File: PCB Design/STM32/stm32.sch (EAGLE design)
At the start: 68 parts, among them IC1 NCP1117ST50T3G, Q1 8MHz, T1 SFH303, T2 SFH303, T3 SFH303, T4 SFH303, U1 STM32F103RET6, U2 MCP1700T-3302E/TT, U3 MCP1700T-3302E/TT, U4 MPU-6050, U5 TB6612FNG, X1 22-23-2031

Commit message: first darft
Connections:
- net IR_OUT1: now also U1.PC9; no longer U1.PC6
- net IR_OUT2: now also U1.PC8; no longer U1.PC7
- net IR_OUT3: now also U1.PC7; no longer U1.PC8
- net IR_OUT4: now also U1.PC6; no longer U1.PC9
- net M1CA: now also JP4.6; no longer JP3.6
- net M1CB: now also JP4.5; no longer JP3.5
- net M2CA: now also JP3.6, U1.PB15; no longer JP4.6, U1.PB14
- net M2CB: now also JP3.5, U1.PB14; no longer JP4.5, U1.PB15
- net USART1_RX: now also U$1.6; no longer U$1.4
- net USART1_TX: now also U$1.4; no longer U$1.6
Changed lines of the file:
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@@
+</segment>
+<segment>
+<wire x1="99.06" y1="172.72" x2="109.22" y2="172.72" width="0.1524" layer="91"/>
+<label x="99.06" y="172.72" size="1.778" layer="95"/>
+<pinref part="U$1" gate="G$1" pin="6"/>
+</segment>
+</net>
+<net name="USART1_TX" class="0">
+<segment>
+<wire x1="162.56" y1="215.9" x2="147.32" y2="215.9" width="0.1524" layer="91"/>
+<label x="142.24" y="215.9" size="1.778" layer="95"/>
+<pinref part="U1" gate="A" pin="PA9"/>
 </segment>
 <segment>
@@
 <label x="99.06" y="175.26" size="1.778" layer="95"/>
 <pinref part="U$1" gate="G$1" pin="4"/>
-</segment>
-</net>
-<net name="USART1_TX" class="0">
-<segment>
-<wire x1="162.56" y1="215.9" x2="147.32" y2="215.9" width="0.1524" layer="91"/>
-<label x="142.24" y="215.9" size="1.778" layer="95"/>
-<pinref part="U1" gate="A" pin="PA9"/>
-</segment>
-<segment>
-<wire x1="99.06" y1="172.72" x2="109.22" y2="172.72" width="0.1524" layer="91"/>
-<label x="99.06" y="172.72" size="1.778" layer="95"/>
-<pinref part="U$1" gate="G$1" pin="6"/>
 </segment>
 </net>
@@
 </segment>
 <segment>
+<pinref part="U1" gate="A" pin="PC8"/>
+<wire x1="223.52" y1="226.06" x2="238.76" y2="226.06" width="0.1524" layer="91"/>
+<label x="228.6" y="226.06" size="1.778" layer="95"/>
+</segment>
+</net>
+<net name="IR_OUT1" class="0">
+<segment>
+<pinref part="R11" gate="G$1" pin="2"/>
+<wire x1="259.08" y1="236.22" x2="259.08" y2="226.06" width="0.1524" layer="91"/>
+<label x="259.08" y="228.6" size="1.778" layer="95"/>
+</segment>
+<segment>
+<pinref part="U1" gate="A" pin="PC9"/>
+<wire x1="223.52" y1="223.52" x2="238.76" y2="223.52" width="0.1524" layer="91"/>
+<label x="228.6" y="223.52" size="1.778" layer="95"/>
+</segment>
+</net>
+<net name="IR_OUT3" class="0">
+<segment>
+<pinref part="R13" gate="G$1" pin="2"/>
+<wire x1="304.8" y1="236.22" x2="304.8" y2="226.06" width="0.1524" layer="91"/>
+<label x="304.8" y="228.6" size="1.778" layer="95"/>
+</segment>
+<segment>
 <pinref part="U1" gate="A" pin="PC7"/>
 <wire x1="223.52" y1="228.6" x2="238.76" y2="228.6" width="0.1524" layer="91"/>
 <label x="228.6" y="228.6" size="1.778" layer="95"/>
-</segment>
-</net>
-<net name="IR_OUT1" class="0">
-<segment>
-<pinref part="R11" gate="G$1" pin="2"/>
-<wire x1="259.08" y1="236.22" x2="259.08" y2="226.06" width="0.1524" layer="91"/>
-<label x="259.08" y="228.6" size="1.778" layer="95"/>
-</segment>
-<segment>
-<pinref part="U1" gate="A" pin="PC6"/>
-<wire x1="223.52" y1="231.14" x2="238.76" y2="231.14" width="0.1524" layer="91"/>
-<label x="228.6" y="231.14" size="1.778" layer="95"/>
-</segment>
-</net>
-<net name="IR_OUT3" class="0">
-<segment>
-<pinref part="R13" gate="G$1" pin="2"/>
-<wire x1="304.8" y1="236.22" x2="304.8" y2="226.06" width="0.1524" layer="91"/>
-<label x="304.8" y="228.6" size="1.778" layer="95"/>
-</segment>
-<segment>
-<pinref part="U1" gate="A" pin="PC8"/>
-<wire x1="223.52" y1="226.06" x2="238.76" y2="226.06" width="0.1524" layer="91"/>
-<label x="228.6" y="226.06" size="1.778" layer="95"/>
 </segment>
 </net>
@@
 </segment>
 <segment>
-<pinref part="U1" gate="A" pin="PC9"/>
-<wire x1="223.52" y1="223.52" x2="238.76" y2="223.52" width="0.1524" layer="91"/>
-<label x="228.6" y="223.52" size="1.778" layer="95"/>
+<pinref part="U1" gate="A" pin="PC6"/>
+<wire x1="223.52" y1="231.14" x2="238.76" y2="231.14" width="0.1524" layer="91"/>
+<label x="228.6" y="231.14" size="1.778" layer="95"/>
 </segment>
 </net>
@@
 <net name="M1CB" class="0">
 <segment>
+<wire x1="162.56" y1="162.56" x2="147.32" y2="162.56" width="0.1524" layer="91"/>
+<label x="154.94" y="162.56" size="1.778" layer="95" rot="MR0"/>
+<pinref part="U1" gate="A" pin="PB13"/>
+</segment>
+<segment>
+<pinref part="JP4" gate="G$1" pin="5"/>
+<wire x1="401.32" y1="109.22" x2="393.7" y2="109.22" width="0.1524" layer="91"/>
+<label x="393.7" y="106.68" size="1.778" layer="95"/>
+</segment>
+</net>
+<net name="M1CA" class="0">
+<segment>
+<wire x1="162.56" y1="165.1" x2="147.32" y2="165.1" width="0.1524" layer="91"/>
+<label x="154.94" y="165.1" size="1.778" layer="95" rot="MR0"/>
+<pinref part="U1" gate="A" pin="PB12"/>
+</segment>
+<segment>
+<pinref part="JP4" gate="G$1" pin="6"/>
+<wire x1="416.56" y1="109.22" x2="424.18" y2="109.22" width="0.1524" layer="91"/>
+<label x="419.1" y="106.68" size="1.778" layer="95"/>
+</segment>
+</net>
+<net name="M2CA" class="0">
+<segment>
+<pinref part="JP3" gate="G$1" pin="6"/>
+<wire x1="416.56" y1="129.54" x2="424.18" y2="129.54" width="0.1524" layer="91"/>
+<label x="419.1" y="127" size="1.778" layer="95"/>
+</segment>
+<segment>
+<wire x1="162.56" y1="157.48" x2="147.32" y2="157.48" width="0.1524" layer="91"/>
+<label x="154.94" y="157.48" size="1.778" layer="95" rot="MR0"/>
+<pinref part="U1" gate="A" pin="PB15"/>
+</segment>
+</net>
+<net name="M2CB" class="0">
+<segment>
 <pinref part="JP3" gate="G$1" pin="5"/>
 <wire x1="401.32" y1="129.54" x2="393.7" y2="129.54" width="0.1524" layer="91"/>
@@
 </segment>
 <segment>
-<wire x1="162.56" y1="162.56" x2="147.32" y2="162.56" width="0.1524" layer="91"/>
-<label x="154.94" y="162.56" size="1.778" layer="95" rot="MR0"/>
-<pinref part="U1" gate="A" pin="PB13"/>
-</segment>
-</net>
-<net name="M1CA" class="0">
-<segment>
-<pinref part="JP3" gate="G$1" pin="6"/>
-<wire x1="416.56" y1="129.54" x2="424.18" y2="129.54" width="0.1524" layer="91"/>
-<label x="419.1" y="127" size="1.778" layer="95"/>
-</segment>
-<segment>
-<wire x1="162.56" y1="165.1" x2="147.32" y2="165.1" width="0.1524" layer="91"/>
-<label x="154.94" y="165.1" size="1.778" layer="95" rot="MR0"/>
-<pinref part="U1" gate="A" pin="PB12"/>
-</segment>
-</net>
-<net name="M2CA" class="0">
-<segment>
-<pinref part="JP4" gate="G$1" pin="6"/>
-<wire x1="416.56" y1="109.22" x2="424.18" y2="109.22" width="0.1524" layer="91"/>
-<label x="419.1" y="106.68" size="1.778" layer="95"/>
-</segment>
-<segment>
 <wire x1="162.56" y1="160.02" x2="147.32" y2="160.02" width="0.1524" layer="91"/>
 <label x="154.94" y="160.02" size="1.778" layer="95" rot="MR0"/>
@@
 </segment>
 </net>
-<net name="M2CB" class="0">
-<segment>
-<pinref part="JP4" gate="G$1" pin="5"/>
-<wire x1="401.32" y1="109.22" x2="393.7" y2="109.22" width="0.1524" layer="91"/>
-<label x="393.7" y="106.68" size="1.778" layer="95"/>
-</segment>
-<segment>
-<wire x1="162.56" y1="157.48" x2="147.32" y2="157.48" width="0.1524" layer="91"/>
-<label x="154.94" y="157.48" size="1.778" layer="95" rot="MR0"/>
-<pinref part="U1" gate="A" pin="PB15"/>
-</segment>
-</net>

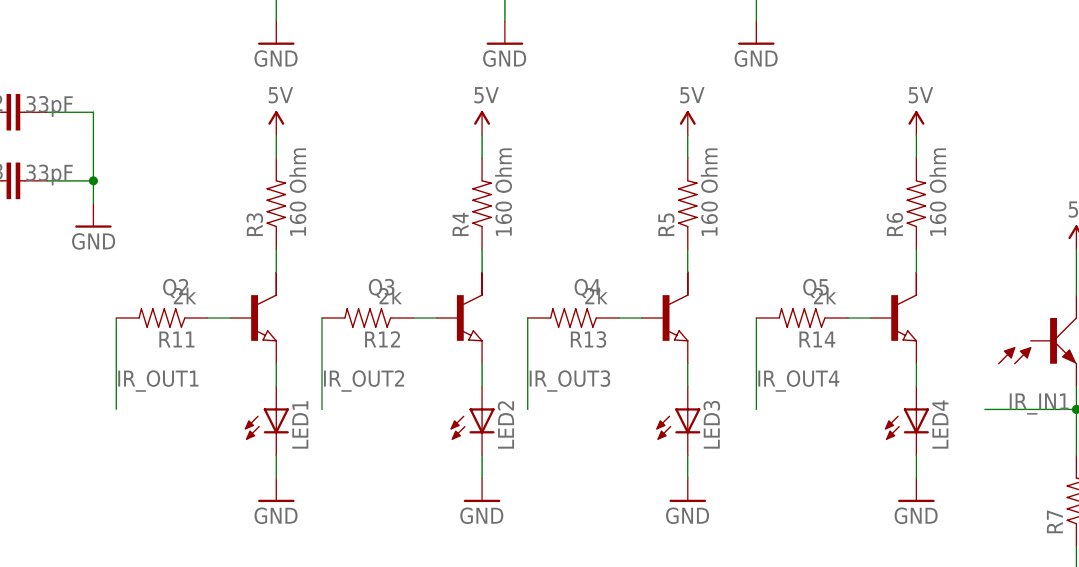
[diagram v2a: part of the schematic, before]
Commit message: changed the transistor to BC847 with package SOT23
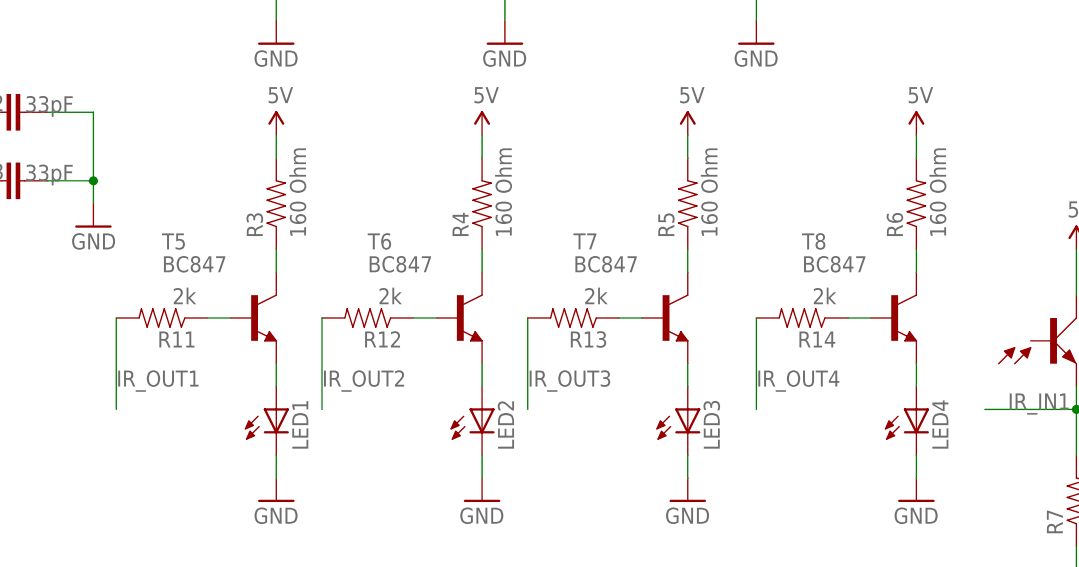
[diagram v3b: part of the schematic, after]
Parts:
- removed Q2, Q3, Q4, Q5: (no value), semicon-smd-ipc:NPN-TRANSISTIOR-2COLSOT89
- added T5, T6, T7, T8: BC847, transistor:BC847
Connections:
- net N$14: now also T8.E; no longer Q5.E
- net N$15: now also T5.C; no longer Q2.C
- net N$16: now also T7.C; no longer Q4.C
- net N$17: now also T8.C; no longer Q5.C
- net N$22: now also T8.B; no longer Q5.B
- net N$23: now also T7.B; no longer Q4.B
- net N$24: now also T6.B; no longer Q3.B
- net N$25: now also T5.B; no longer Q2.B
- net N$3: now also T6.C; no longer Q3.C
- net N$4: now also T5.E; no longer Q2.E
- net N$5: now also T6.E; no longer Q3.E
- net N$7: now also T7.E; no longer Q4.E
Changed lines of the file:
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@@
 <part name="R6" library="SparkFun-Resistors" deviceset="RESISTOR" device="0805-RES" value="160 Ohm"/>
 <part name="R10" library="SparkFun-Resistors" deviceset="RESISTOR" device="0805-RES" value="42 Ohm"/>
-<part name="Q2" library="semicon-smd-ipc" deviceset="NPN-TRANSISTIOR-2COL" device="SOT89"/>
-<part name="Q3" library="semicon-smd-ipc" deviceset="NPN-TRANSISTIOR-2COL" device="SOT89"/>
-<part name="Q4" library="semicon-smd-ipc" deviceset="NPN-TRANSISTIOR-2COL" device="SOT89"/>
-<part name="Q5" library="semicon-smd-ipc" deviceset="NPN-TRANSISTIOR-2COL" device="SOT89"/>
 <part name="GND11" library="SparkFun-Aesthetics" deviceset="GND" device=""/>
 <part name="GND14" library="SparkFun-Aesthetics" deviceset="GND" device=""/>
@@
 <part name="GND39" library="SparkFun-Aesthetics" deviceset="GND" device=""/>
 <part name="U$1" library="SparkFun-Connectors" deviceset="M04X2" device=""/>
+<part name="T5" library="transistor" deviceset="BC847" device=""/>
+<part name="T6" library="transistor" deviceset="BC847" device=""/>
+<part name="T7" library="transistor" deviceset="BC847" device=""/>
+<part name="T8" library="transistor" deviceset="BC847" device=""/>
 </parts>
 <sheets>
@@
 <instance part="R6" gate="G$1" x="347.98" y="248.92" rot="R90"/>
 <instance part="R10" gate="G$1" x="429.26" y="215.9" rot="R90"/>
-<instance part="Q2" gate="G$1" x="274.32" y="236.22"/>
-<instance part="Q3" gate="G$1" x="297.18" y="236.22"/>
-<instance part="Q4" gate="G$1" x="320.04" y="236.22"/>
-<instance part="Q5" gate="G$1" x="345.44" y="236.22"/>
 <instance part="GND11" gate="1" x="276.86" y="215.9"/>
 <instance part="GND14" gate="1" x="299.72" y="215.9"/>
@@
 <instance part="GND39" gate="1" x="101.6" y="119.38"/>
 <instance part="U$1" gate="G$1" x="91.44" y="172.72"/>
+<instance part="T5" gate="G$1" x="274.32" y="236.22"/>
+<instance part="T6" gate="G$1" x="297.18" y="236.22"/>
+<instance part="T7" gate="G$1" x="320.04" y="236.22"/>
+<instance part="T8" gate="G$1" x="345.44" y="236.22"/>
 </instances>
 <busses>
@@
 <net name="N$22" class="0">
 <segment>
-<pinref part="Q5" gate="G$1" pin="B"/>
 <pinref part="R14" gate="G$1" pin="1"/>
 <wire x1="342.9" y1="236.22" x2="340.36" y2="236.22" width="0.1524" layer="91"/>
+<pinref part="T8" gate="G$1" pin="B"/>
 </segment>
 </net>
 <net name="N$23" class="0">
 <segment>
-<pinref part="Q4" gate="G$1" pin="B"/>
 <pinref part="R13" gate="G$1" pin="1"/>
 <wire x1="317.5" y1="236.22" x2="314.96" y2="236.22" width="0.1524" layer="91"/>
+<pinref part="T7" gate="G$1" pin="B"/>
 </segment>
 </net>
 <net name="N$24" class="0">
 <segment>
-<pinref part="Q3" gate="G$1" pin="B"/>
 <pinref part="R12" gate="G$1" pin="1"/>
 <wire x1="294.64" y1="236.22" x2="292.1" y2="236.22" width="0.1524" layer="91"/>
+<pinref part="T6" gate="G$1" pin="B"/>
 </segment>
 </net>
 <net name="N$25" class="0">
 <segment>
-<pinref part="Q2" gate="G$1" pin="B"/>
 <pinref part="R11" gate="G$1" pin="1"/>
 <wire x1="271.78" y1="236.22" x2="269.24" y2="236.22" width="0.1524" layer="91"/>
+<pinref part="T5" gate="G$1" pin="B"/>
 </segment>
 </net>
@@
 <net name="N$3" class="0">
 <segment>
-<pinref part="Q3" gate="G$1" pin="C"/>
 <pinref part="R4" gate="G$1" pin="1"/>
 <wire x1="299.72" y1="243.84" x2="299.72" y2="241.3" width="0.1524" layer="91"/>
+<pinref part="T6" gate="G$1" pin="C"/>
 </segment>
 </net>
 <net name="N$4" class="0">
 <segment>
-<pinref part="Q2" gate="G$1" pin="E"/>
 <pinref part="LED1" gate="G$1" pin="A"/>
 <wire x1="276.86" y1="231.14" x2="276.86" y2="228.6" width="0.1524" layer="91"/>
+<pinref part="T5" gate="G$1" pin="E"/>
 </segment>
 </net>
 <net name="N$5" class="0">
 <segment>
-<pinref part="Q3" gate="G$1" pin="E"/>
 <pinref part="LED2" gate="G$1" pin="A"/>
 <wire x1="299.72" y1="231.14" x2="299.72" y2="228.6" width="0.1524" layer="91"/>
+<pinref part="T6" gate="G$1" pin="E"/>
 </segment>
 </net>
 <net name="N$7" class="0">
 <segment>
-<pinref part="Q4" gate="G$1" pin="E"/>
 <pinref part="LED3" gate="G$1" pin="A"/>
 <wire x1="322.58" y1="231.14" x2="322.58" y2="228.6" width="0.1524" layer="91"/>
+<pinref part="T7" gate="G$1" pin="E"/>
 </segment>
 </net>
 <net name="N$14" class="0">
 <segment>
-<pinref part="Q5" gate="G$1" pin="E"/>
 <pinref part="LED4" gate="G$1" pin="A"/>
 <wire x1="347.98" y1="231.14" x2="347.98" y2="228.6" width="0.1524" layer="91"/>
+<pinref part="T8" gate="G$1" pin="E"/>
 </segment>
 </net>
@@
 <segment>
 <pinref part="R3" gate="G$1" pin="1"/>
-<pinref part="Q2" gate="G$1" pin="C"/>
 <wire x1="276.86" y1="243.84" x2="276.86" y2="241.3" width="0.1524" layer="91"/>
+<pinref part="T5" gate="G$1" pin="C"/>
 </segment>
 </net>
@@
 <segment>
 <pinref part="R5" gate="G$1" pin="1"/>
-<pinref part="Q4" gate="G$1" pin="C"/>
 <wire x1="322.58" y1="243.84" x2="322.58" y2="241.3" width="0.1524" layer="91"/>
+<pinref part="T7" gate="G$1" pin="C"/>
 </segment>
 </net>
@@
 <segment>
 <pinref part="R6" gate="G$1" pin="1"/>
-<pinref part="Q5" gate="G$1" pin="C"/>
 <wire x1="347.98" y1="243.84" x2="347.98" y2="241.3" width="0.1524" layer="91"/>
-</segment>
-</net>
+<pinref part="T8" gate="G$1" pin="C"/>
+</segment>
+</net>

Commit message: third draft
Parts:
- C12, C13: value 33pF -> 10pF
- Q1: value 8MHz -> ABM3B-8.000MHZ-10-1UT; device SparkFun2:CRYSTAL5X3 -> SparkFun-FreqCtrl:CRYSTAL5X3
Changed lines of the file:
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@@
 </classes>
 <parts>
-<part name="Q1" library="SparkFun2" deviceset="CRYSTAL" device="5X3" value="8MHz"/>
+<part name="Q1" library="SparkFun-FreqCtrl" deviceset="CRYSTAL" device="5X3" value="ABM3B-8.000MHZ-10-1UT"/>
 <part name="GND10" library="SparkFun" deviceset="GND" device=""/>
-<part name="C12" library="SparkFun-Capacitors" deviceset="CAP" device="0805" value="33pF"/>
-<part name="C13" library="SparkFun-Capacitors" deviceset="CAP" device="0805" value="33pF"/>
+<part name="C12" library="SparkFun-Capacitors" deviceset="CAP" device="0805" value="10pF"/>
+<part name="C13" library="SparkFun-Capacitors" deviceset="CAP" device="0805" value="10pF"/>
 <part name="P+1" library="SparkFun" deviceset="VCC" device=""/>
 <part name="GND1" library="SparkFun" deviceset="GND" device=""/>

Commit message: crystal update
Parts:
- Q1: device SparkFun-FreqCtrl:CRYSTAL5X3 -> SparkFun-FreqCtrl:CRYSTAL-GROUNDED
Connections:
- net GND: now also Q1.3
- net N$2: now also C12.2, U1.PD0_OSC_IN; no longer C13.2, U1.PD1_OSC_OUT
- net N$6: now also C13.2, U1.PD1_OSC_OUT; no longer C12.2, U1.PD0_OSC_IN
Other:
- moved on the sheet: C12, C13
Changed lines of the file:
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@@
 </classes>
 <parts>
-<part name="Q1" library="SparkFun-FreqCtrl" deviceset="CRYSTAL" device="5X3" value="ABM3B-8.000MHZ-10-1UT"/>
+<part name="Q1" library="SparkFun-FreqCtrl" deviceset="CRYSTAL-GROUNDED" device="" value="ABM3B-8.000MHZ-10-1UT"/>
 <part name="GND10" library="SparkFun" deviceset="GND" device=""/>
 <part name="C12" library="SparkFun-Capacitors" deviceset="CAP" device="0805" value="10pF"/>
@@
 </plain>
 <instances>
-<instance part="Q1" gate="G$1" x="236.22" y="255.27" smashed="yes" rot="R90">
-<attribute name="NAME" x="238.76" y="256.54" size="1.778" layer="95"/>
-<attribute name="VALUE" x="238.76" y="254" size="1.778" layer="96"/>
+<instance part="Q1" gate="G$1" x="231.14" y="254" smashed="yes" rot="MR270">
+<attribute name="NAME" x="233.68" y="252.73" size="1.778" layer="95" rot="MR180"/>
+<attribute name="VALUE" x="233.68" y="255.27" size="1.778" layer="96" rot="MR180"/>
 </instance>
-<instance part="GND10" gate="1" x="256.54" y="246.38" rot="MR0"/>
-<instance part="C12" gate="G$1" x="246.38" y="259.08" smashed="yes" rot="R270">
-<attribute name="NAME" x="242.316" y="259.207" size="1.778" layer="95"/>
-<attribute name="VALUE" x="248.92" y="259.08" size="1.778" layer="96"/>
+<instance part="GND10" gate="1" x="251.46" y="243.84" rot="MR0"/>
+<instance part="C12" gate="G$1" x="238.76" y="259.08" smashed="yes" rot="R270">
+<attribute name="NAME" x="234.696" y="259.207" size="1.778" layer="95"/>
+<attribute name="VALUE" x="241.3" y="259.08" size="1.778" layer="96"/>
 </instance>
-<instance part="C13" gate="G$1" x="246.38" y="251.46" smashed="yes" rot="R270">
-<attribute name="NAME" x="242.316" y="251.587" size="1.778" layer="95"/>
-<attribute name="VALUE" x="248.92" y="251.46" size="1.778" layer="96"/>
+<instance part="C13" gate="G$1" x="238.76" y="248.92" smashed="yes" rot="R270">
+<attribute name="NAME" x="234.696" y="249.047" size="1.778" layer="95"/>
+<attribute name="VALUE" x="241.3" y="248.92" size="1.778" layer="96"/>
 </instance>
 <instance part="P+1" gate="1" x="99.06" y="226.06"/>
@@
 <net name="GND" class="0">
 <segment>
-<wire x1="251.46" y1="259.08" x2="256.54" y2="259.08" width="0.1524" layer="91"/>
-<wire x1="256.54" y1="259.08" x2="256.54" y2="251.46" width="0.1524" layer="91"/>
-<wire x1="256.54" y1="251.46" x2="256.54" y2="248.92" width="0.1524" layer="91"/>
-<wire x1="251.46" y1="251.46" x2="256.54" y2="251.46" width="0.1524" layer="91"/>
-<junction x="256.54" y="251.46"/>
+<wire x1="251.46" y1="259.08" x2="251.46" y2="254" width="0.1524" layer="91"/>
+<pinref part="GND10" gate="1" pin="GND"/>
+<wire x1="251.46" y1="254" x2="251.46" y2="248.92" width="0.1524" layer="91"/>
+<pinref part="Q1" gate="G$1" pin="3"/>
+<wire x1="251.46" y1="248.92" x2="251.46" y2="246.38" width="0.1524" layer="91"/>
+<wire x1="236.22" y1="254" x2="251.46" y2="254" width="0.1524" layer="91"/>
+<junction x="251.46" y="254"/>
 <pinref part="C12" gate="G$1" pin="1"/>
-<pinref part="GND10" gate="1" pin="GND"/>
+<wire x1="243.84" y1="259.08" x2="251.46" y2="259.08" width="0.1524" layer="91"/>
 <pinref part="C13" gate="G$1" pin="1"/>
+<wire x1="243.84" y1="248.92" x2="251.46" y2="248.92" width="0.1524" layer="91"/>
 </segment>
 <segment>
@@
 </segment>
 </net>
-<net name="N$6" class="0">
-<segment>
-<wire x1="236.22" y1="259.08" x2="243.84" y2="259.08" width="0.1524" layer="91"/>
-<wire x1="236.22" y1="257.81" x2="236.22" y2="259.08" width="0.1524" layer="91"/>
-<junction x="236.22" y="259.08"/>
-<pinref part="Q1" gate="G$1" pin="2"/>
-<pinref part="C12" gate="G$1" pin="2"/>
-<pinref part="U1" gate="A" pin="PD0_OSC_IN"/>
-<wire x1="223.52" y1="256.54" x2="236.22" y2="259.08" width="0.1524" layer="91"/>
-</segment>
-</net>
-<net name="N$2" class="0">
-<segment>
-<wire x1="236.22" y1="252.73" x2="236.22" y2="251.46" width="0.1524" layer="91"/>
-<wire x1="236.22" y1="251.46" x2="243.84" y2="251.46" width="0.1524" layer="91"/>
-<pinref part="Q1" gate="G$1" pin="1"/>
-<pinref part="C13" gate="G$1" pin="2"/>
-<pinref part="U1" gate="A" pin="PD1_OSC_OUT"/>
-<wire x1="236.22" y1="251.46" x2="223.52" y2="254" width="0.1524" layer="91"/>
-<junction x="236.22" y="251.46"/>
-</segment>
-</net>
 <net name="JTAG-TMS" class="0">
 <segment>
@@
 </segment>
 </net>
+<net name="N$6" class="0">
+<segment>
+<pinref part="U1" gate="A" pin="PD1_OSC_OUT"/>
+<wire x1="223.52" y1="254" x2="226.06" y2="254" width="0.1524" layer="91"/>
+<wire x1="226.06" y1="254" x2="226.06" y2="248.92" width="0.1524" layer="91"/>
+<pinref part="Q1" gate="G$1" pin="2"/>
+<wire x1="231.14" y1="248.92" x2="226.06" y2="248.92" width="0.1524" layer="91"/>
+<wire x1="231.14" y1="251.46" x2="231.14" y2="248.92" width="0.1524" layer="91"/>
+<pinref part="C13" gate="G$1" pin="2"/>
+<wire x1="236.22" y1="248.92" x2="231.14" y2="248.92" width="0.1524" layer="91"/>
+<junction x="231.14" y="248.92"/>
+</segment>
+</net>
+<net name="N$2" class="0">
+<segment>
+<pinref part="U1" gate="A" pin="PD0_OSC_IN"/>
+<wire x1="223.52" y1="256.54" x2="226.06" y2="256.54" width="0.1524" layer="91"/>
+<wire x1="226.06" y1="256.54" x2="226.06" y2="259.08" width="0.1524" layer="91"/>
+<wire x1="226.06" y1="259.08" x2="231.14" y2="259.08" width="0.1524" layer="91"/>
+<pinref part="Q1" gate="G$1" pin="1"/>
+<wire x1="231.14" y1="259.08" x2="231.14" y2="256.54" width="0.1524" layer="91"/>
+<pinref part="C12" gate="G$1" pin="2"/>
+<wire x1="231.14" y1="259.08" x2="236.22" y2="259.08" width="0.1524" layer="91"/>
+<junction x="231.14" y="259.08"/>
+</segment>
+</net>
